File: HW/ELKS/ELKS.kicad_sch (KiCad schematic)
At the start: 4 parts

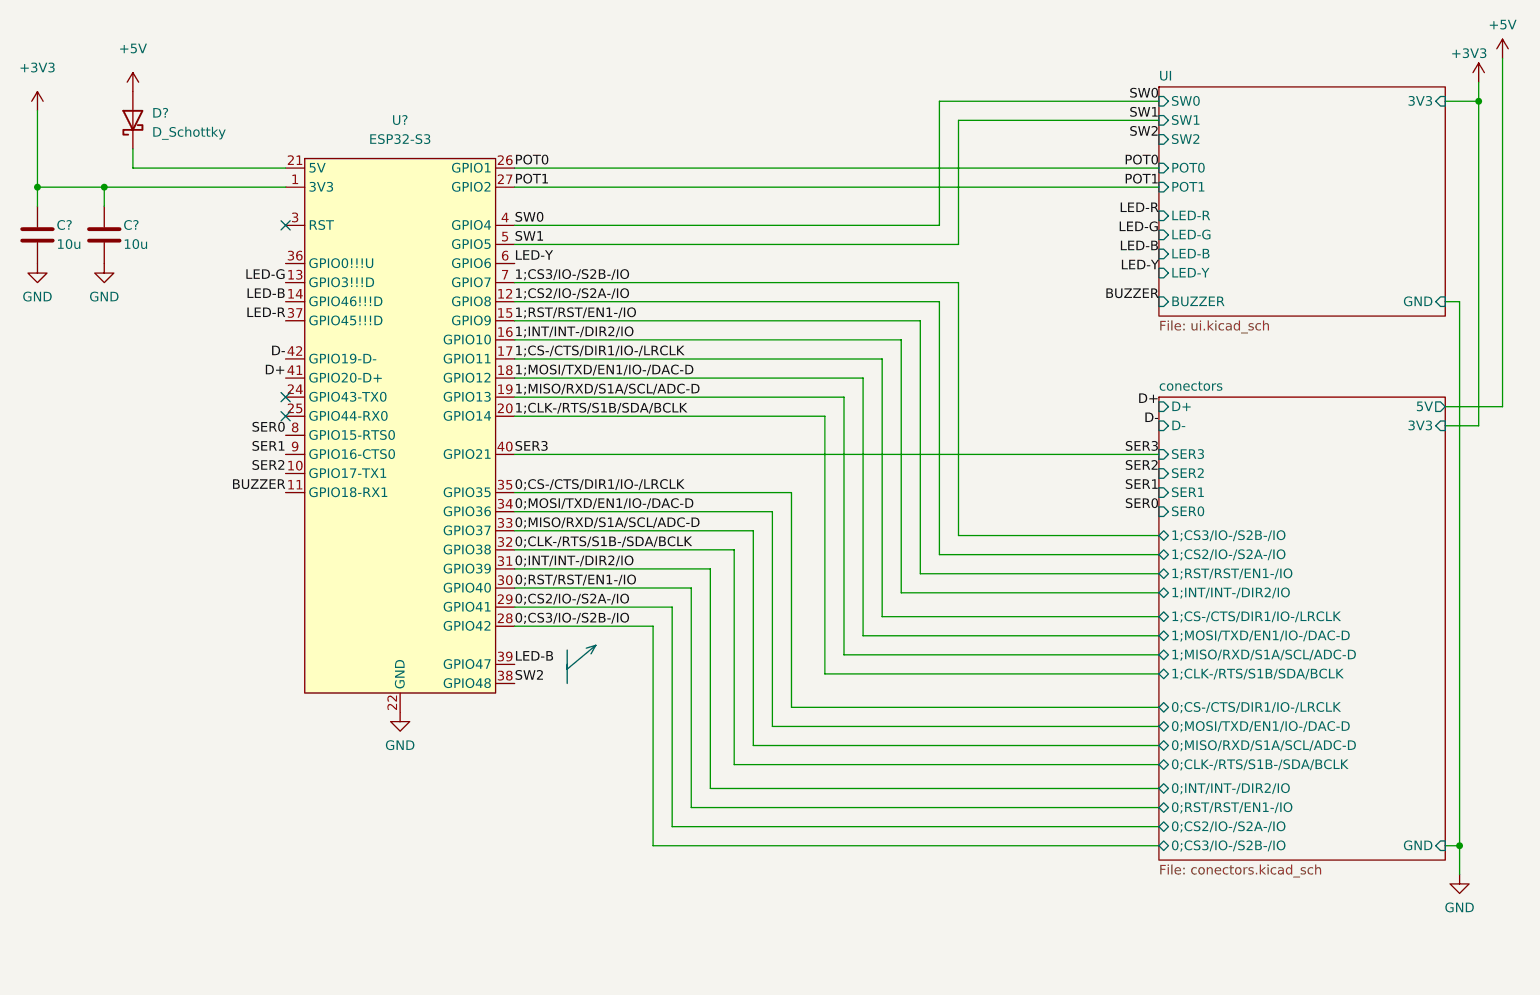
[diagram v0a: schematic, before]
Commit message: Laskakit I2C connector
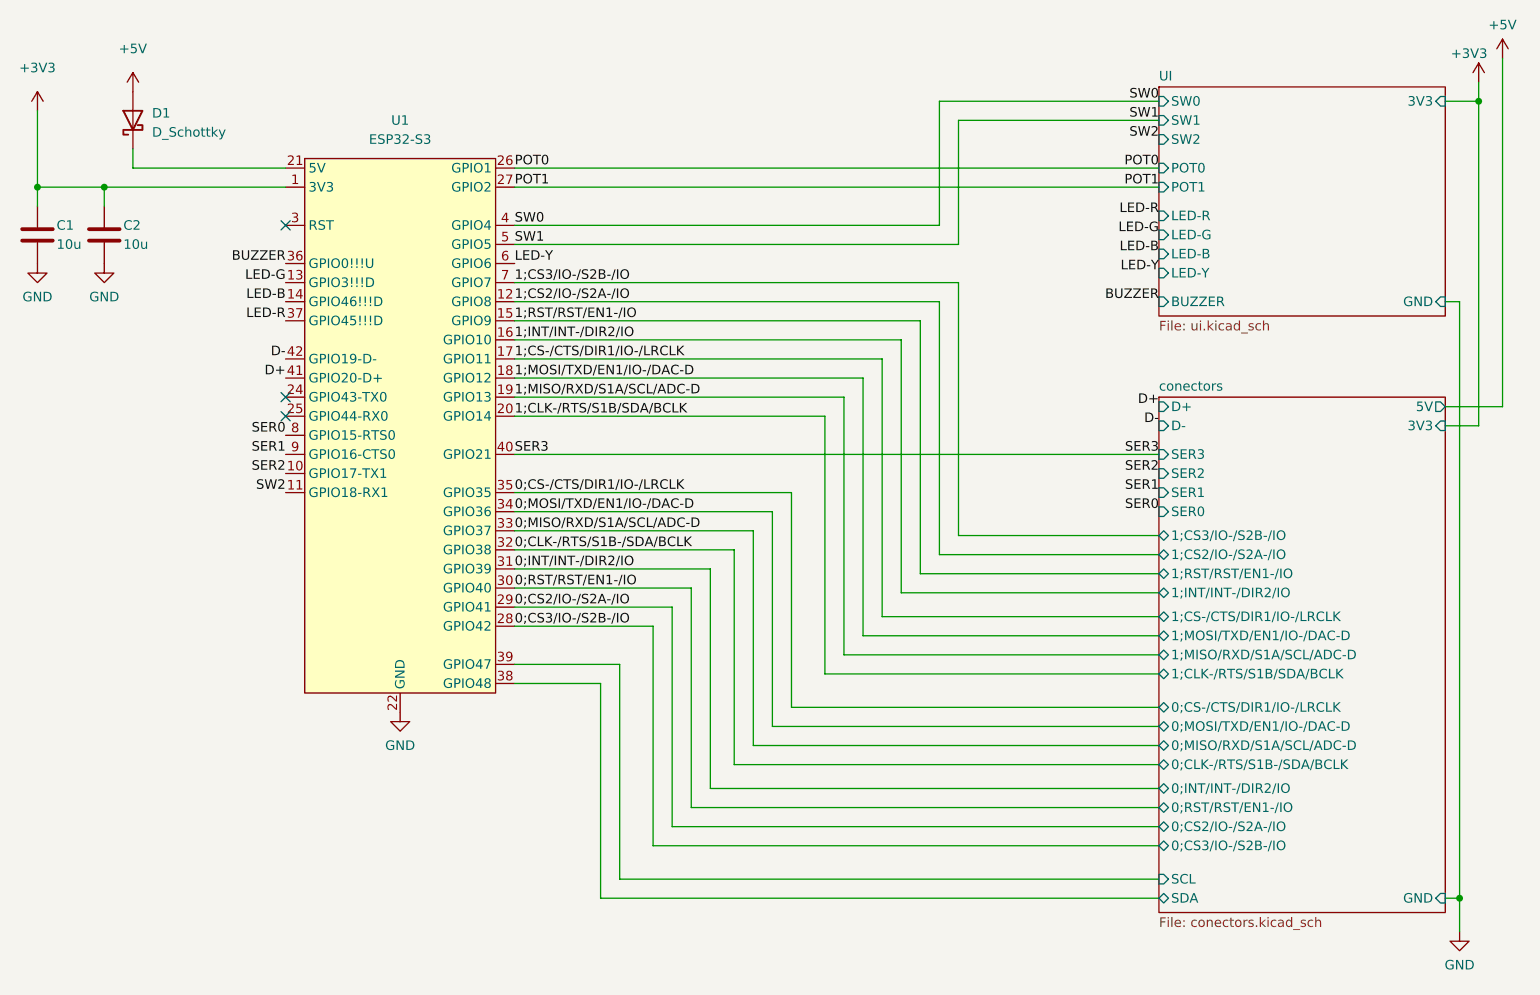
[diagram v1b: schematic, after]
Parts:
- gave numbers to parts that had none: 4
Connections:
- net BUZZER: now also U1.36 (GPIO0!!!U); no longer U1.11 (GPIO18-RX1)
- net LED-B: no longer U1.39 (GPIO47)
- net SW2: now also U1.11 (GPIO18-RX1); no longer U1.38 (GPIO48)
- new net conectors/SCL: U1.39 (GPIO47)
- new net conectors/SDA: U1.38 (GPIO48)
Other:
- sheet conectors ports: added SCL, SDA; removed none

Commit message: KiCad PDB
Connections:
- net +3V3: now also U1.2 (3V3)
- net 0;CLK-/RTS/S1B-/SDA/BCLK: now also U1.35 (GPIO35); no longer U1.32 (GPIO38)
- net 0;CS-/CTS/DIR1/IO-/LRCLK: now also U1.29 (GPIO41); no longer U1.35 (GPIO35)
- net 0;CS2/IO-/S2A-/IO: now also U1.30 (GPIO40); no longer U1.29 (GPIO41)
- net 0;INT/INT-/DIR2/IO: now also U1.34 (GPIO36); no longer U1.31 (GPIO39)
- net 0;MOSI/TXD/EN1/IO-/DAC-D: now also U1.31 (GPIO39); no longer U1.34 (GPIO36)
- net 0;RST/RST/EN1-/IO: now also U1.32 (GPIO38); no longer U1.30 (GPIO40)
- net 1;CLK-/RTS/S1B/SDA/BCLK: now also U1.17 (GPIO11); no longer U1.20 (GPIO14)
- net 1;CS-/CTS/DIR1/IO-/LRCLK: now also U1.20 (GPIO14); no longer U1.17 (GPIO11)
- net 1;MISO/RXD/S1A/SCL/ADC-D: now also U1.18 (GPIO12); no longer U1.19 (GPIO13)
- net 1;MOSI/TXD/EN1/IO-/DAC-D: now also U1.19 (GPIO13); no longer U1.18 (GPIO12)
- net GND: now also U1.23 (GND), U1.43 (GND), U1.44 (GND)
- net POT0: now also U1.27 (GPIO2); no longer U1.26 (GPIO1)
- net POT1: now also U1.26 (GPIO1); no longer U1.27 (GPIO2)
- net SER3 renamed I_LED
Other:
- sheet conectors ports: added I-LED; removed SER2, SER3
- note added: "I_LED"

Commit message: Reminders
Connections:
- net 1;CS2/IO-/S2A-/IO: now also U1.15 (GPIO9); no longer U1.12 (GPIO8)
- net 1;CS3/IO-/S2B-/IO: now also U1.16 (GPIO10); no longer U1.7 (GPIO7)
- net 1;INT/INT-/DIR2/IO: now also U1.7 (GPIO7); no longer U1.16 (GPIO10)
- net 1;RST/RST/EN1-/IO: now also U1.12 (GPIO8); no longer U1.15 (GPIO9)
- net LED-Y: now also U1.8 (GPIO15-RTS0); no longer U1.6 (GPIO6)
- net SER0: now also U1.4 (GPIO4); no longer U1.8 (GPIO15-RTS0)
- net SER1: now also U1.5 (GPIO5); no longer U1.9 (GPIO16-CTS0)
- net SW0: now also U1.11 (GPIO18-RX1); no longer U1.4 (GPIO4)
- net SW1: now also U1.9 (GPIO16-CTS0); no longer U1.5 (GPIO5)
- net SW2: now also U1.6 (GPIO6); no longer U1.11 (GPIO18-RX1)
- net SER2: no longer names the net of U1.10 (GPIO17-TX1)
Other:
- moved on the sheet: C1, C2, D1, U1

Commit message: Kikit JLC export
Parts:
- U1: JLCPCB_IGNORE (none) -> true
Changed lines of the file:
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@@
+      (effects (font (size 1.27 1.27)) hide)
+    )
+    (property "JLCPCB_IGNORE" "true" (id 4) (at 102.87 50.8 0)
       (effects (font (size 1.27 1.27)) hide)
     )

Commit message: Fix potentiometers footprints and relocation two component
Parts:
- U1: JLCPCB_IGNORE true -> (none)
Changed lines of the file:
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@@
-      (effects (font (size 1.27 1.27)) hide)
-    )
-    (property "JLCPCB_IGNORE" "true" (id 4) (at 102.87 50.8 0)
       (effects (font (size 1.27 1.27)) hide)
     )
@@
     )
     (path "/8b12a081-f055-41a0-9e9c-5c7d288eeced/b9605053-bf9c-4544-8fa0-996b39633492"
-      (reference "RV1") (unit 1) (value "R_Potentiometer") (footprint "Potentiometer_THT:Potentiometer_Alpha_RD901F-40-00D_Single_Vertical")
+      (reference "RV1") (unit 1) (value "R_Potentiometer") (footprint "Robotarna_KiCad_Library:RK09K113 (ELKS-POT)")
     )
     (path "/8b12a081-f055-41a0-9e9c-5c7d288eeced/cb1bd94d-07df-439d-9087-140826209885"
-      (reference "RV2") (unit 1) (value "R_Potentiometer") (footprint "Potentiometer_THT:Potentiometer_Alpha_RD901F-40-00D_Single_Vertical")
+      (reference "RV2") (unit 1) (value "R_Potentiometer") (footprint "Robotarna_KiCad_Library:RK09K113 (ELKS-POT)")
     )
     (path "/8b12a081-f055-41a0-9e9c-5c7d288eeced/1760ba51-4548-4640-8bbf-208148ebdd33"
